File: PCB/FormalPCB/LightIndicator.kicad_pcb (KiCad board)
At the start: 2 copper layers, 57.5 x 38.2 mm, 32 parts

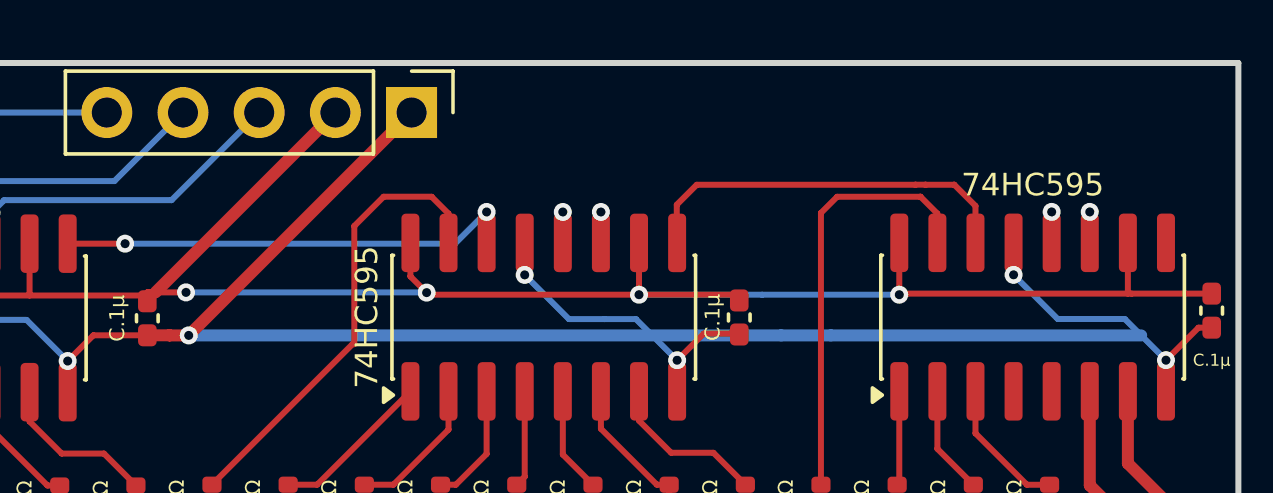
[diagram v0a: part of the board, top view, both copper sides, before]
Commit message: Update complete BOM, edit PCB design, upgrade ConfigCode to PlatformIO
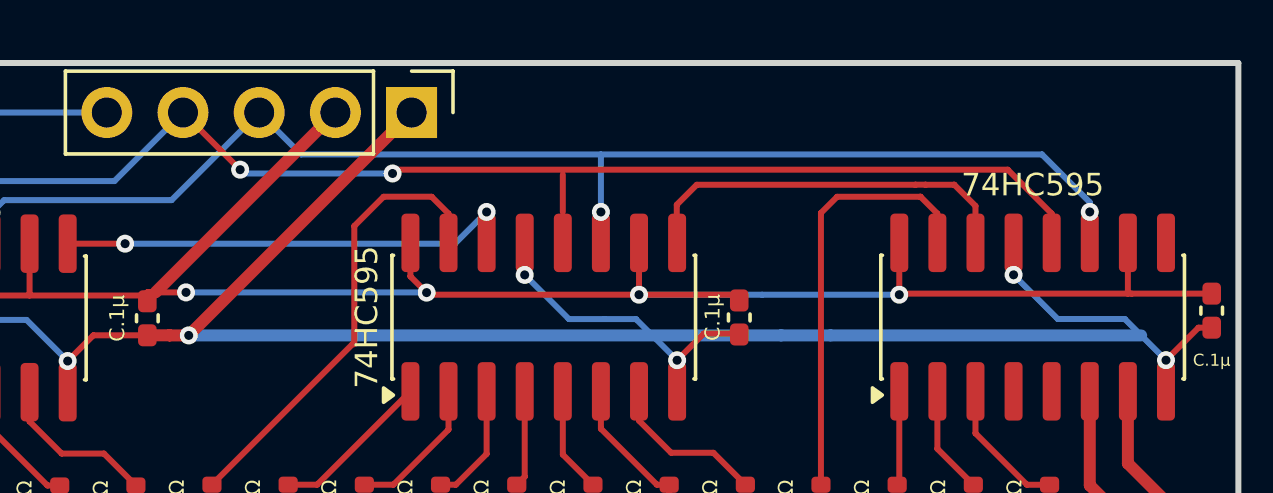
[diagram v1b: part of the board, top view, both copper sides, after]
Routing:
- net 595latch: track 9.04 -> 41.7 mm
- net 595CLK: track 10.3 -> 41.5 mm
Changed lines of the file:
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@@
+	)
+	(segment
+		(start 36.2825 3.048)
+		(end 36.2825 4.966)
+		(width 0.2)
+		(layer "B.Cu")
+		(net "595CLK")
+	)
+	(segment
+		(start 26.289 3.048)
+		(end 50.9849 3.048)
+		(width 0.2)
+		(layer "B.Cu")
+		(net "595CLK")
 	)
 	(segment
 		(start 21.971 4.572)
 		(end 16.388164 4.572)
+		(width 0.2)
+		(layer "B.Cu")
+		(net "595CLK")
+	)
+	(segment
+		(start 24.892 1.651)
+		(end 26.289 3.048)
 		(width 0.2)
 		(layer "B.Cu")
@@
 		(net "595CLK")
 	)
+	(segment
+		(start 50.9849 3.048)
+		(end 52.578 4.6411)
+		(width 0.2)
+		(layer "B.Cu")
+		(net "595CLK")
+	)
+	(segment
+		(start 52.578 4.6411)
+		(end 52.578 4.9642)
+		(width 0.2)
+		(layer "B.Cu")
+		(net "595CLK")
+	)
+	(segment
+		(start 29.337 3.683)
+		(end 29.464 3.556)
+		(width 0.2)
+		(layer "F.Cu")
+		(net "595latch")
+	)
+	(segment
+		(start 49.844599 3.556)
+		(end 51.308 5.019401)
+		(width 0.2)
+		(layer "F.Cu")
+		(net "595latch")
+	)
+	(segment
+		(start 29.464 3.556)
+		(end 49.844599 3.556)
+		(width 0.2)
+		(layer "F.Cu")
+		(net "595latch")
+	)
+	(segment
+		(start 51.308 5.019401)
+		(end 51.308 5.9944)
+		(width 0.2)
+		(layer "F.Cu")
+		(net "595latch")
+	)
+	(segment
+		(start 35.0125 4.966)
+		(end 35.0125 3.7225)
+		(width 0.2)
+		(layer "F.Cu")
+		(net "595latch")
+	)
+	(segment
+		(start 22.352 1.651)
+		(end 24.257 3.556)
+		(width 0.2)
+		(layer "F.Cu")
+		(net "595latch")
+	)
 	(via
-		(at 35.0125 4.966)
+		(at 14.697664 4.9925)
 		(size 0.6)
 		(drill 0.3)
@@
 	)
 	(via
-		(at 51.308 4.9642)
+		(at 24.257 3.556)
 		(size 0.6)
 		(drill 0.3)
@@
 	)
 	(via
-		(at 14.697664 4.9925)
+		(at 29.337 3.683)
 		(size 0.6)
 		(drill 0.3)
@@
 		(width 0.2)
 		(layer "B.Cu")
+		(net "595latch")
+	)
+	(segment
+		(start 24.257 3.556)
+		(end 24.384 3.683)
+		(width 0.2)
+		(layer "B.Cu")
+		(net "595latch")
+	)
+	(segment
+		(start 24.384 3.683)
+		(end 29.337 3.683)
+		(width 0.2)
+		(layer "B.Cu")

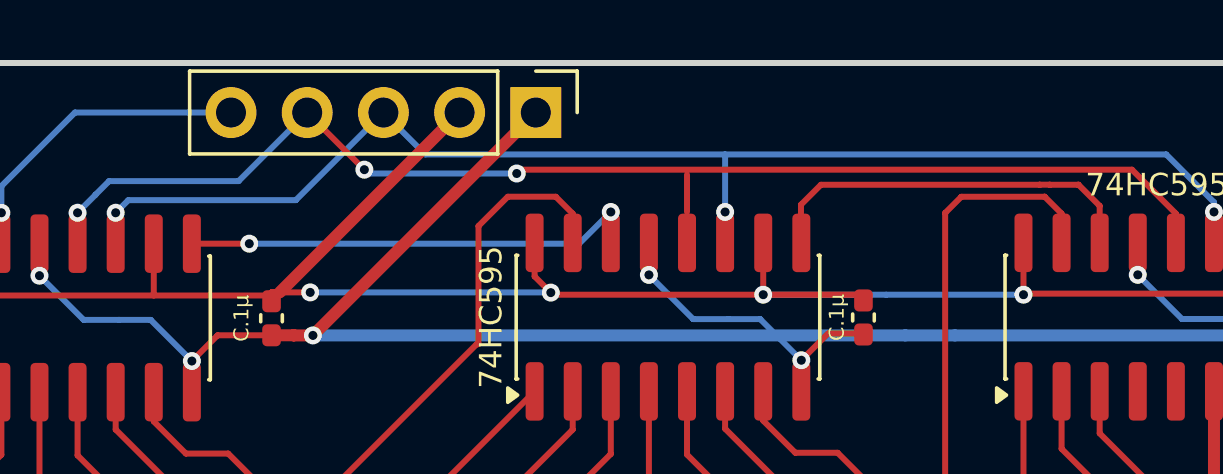
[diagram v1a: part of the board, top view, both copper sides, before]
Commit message: Update PCB and Finish basic IR code and basic integration
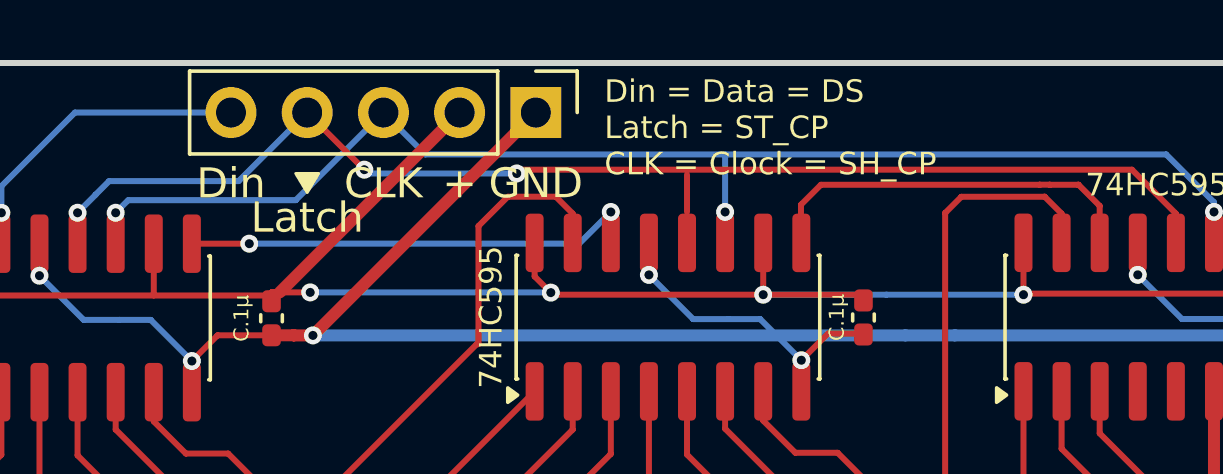
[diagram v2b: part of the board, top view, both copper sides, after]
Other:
- board text added: "+"
- board text added: "CLK"
- board text added: "Din"
- board text added: "Din = Data = DS Latch = ST_CP CLK = Clock = SH_CP"
- board text added: "GND"
- board text added: "Latch"
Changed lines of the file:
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@@
 		(embedded_fonts no)
+	)
+	(gr_poly
+		(pts
+			(xy 21.971 3.683) (xy 22.733 3.683) (xy 22.352 4.318)
+		)
+		(stroke
+			(width 0.1)
+			(type solid)
+		)
+		(fill yes)
+		(layer "F.SilkS")
 	)
 	(gr_rect
@@
 		(layer "Edge.Cuts")
 	)
+	(gr_text "Din = Data = DS\nLatch = ST_CP\nCLK = Clock = SH_CP"
+		(at 32.258 0.508 0)
+		(layer "F.SilkS")
+		(effects
+			(font
+				(size 0.75 0.75)
+				(thickness 0.1)
+			)
+			(justify left top)
+		)
+	)
+	(gr_text "Din"
+		(at 19.812 3.429 0)
+		(layer "F.SilkS")
+		(effects
+			(font
+				(size 1 1)
+				(thickness 0.1)
+			)
+			(justify top)
+		)
+	)
+	(gr_text "Latch"
+		(at 22.352 4.572 0)
+		(layer "F.SilkS")
+		(effects
+			(font
+				(size 1 1)
+				(thickness 0.1)
+			)
+			(justify top)
+		)
+	)
+	(gr_text "CLK"
+		(at 24.892 3.429 0)
+		(layer "F.SilkS")
+		(effects
+			(font
+				(size 1 1)
+				(thickness 0.1)
+			)
+			(justify top)
+		)
+	)
+	(gr_text "+"
+		(at 27.432 3.429 0)
+		(layer "F.SilkS")
+		(effects
+			(font
+				(size 1 1)
+				(thickness 0.1)
+			)
+			(justify top)
+		)
+	)
+	(gr_text "GND"
+		(at 29.972 3.429 0)
+		(layer "F.SilkS")
+		(effects
+			(font
+				(size 1 1)
+				(thickness 0.1)
+			)
+			(justify top)
+		)
+	)
 	(segment
